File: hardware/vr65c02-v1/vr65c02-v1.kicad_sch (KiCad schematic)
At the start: 7 parts, among them J1 Conn_01x06, J2 Conn_01x06, U1 ATMEGA4809, U2 W65C02

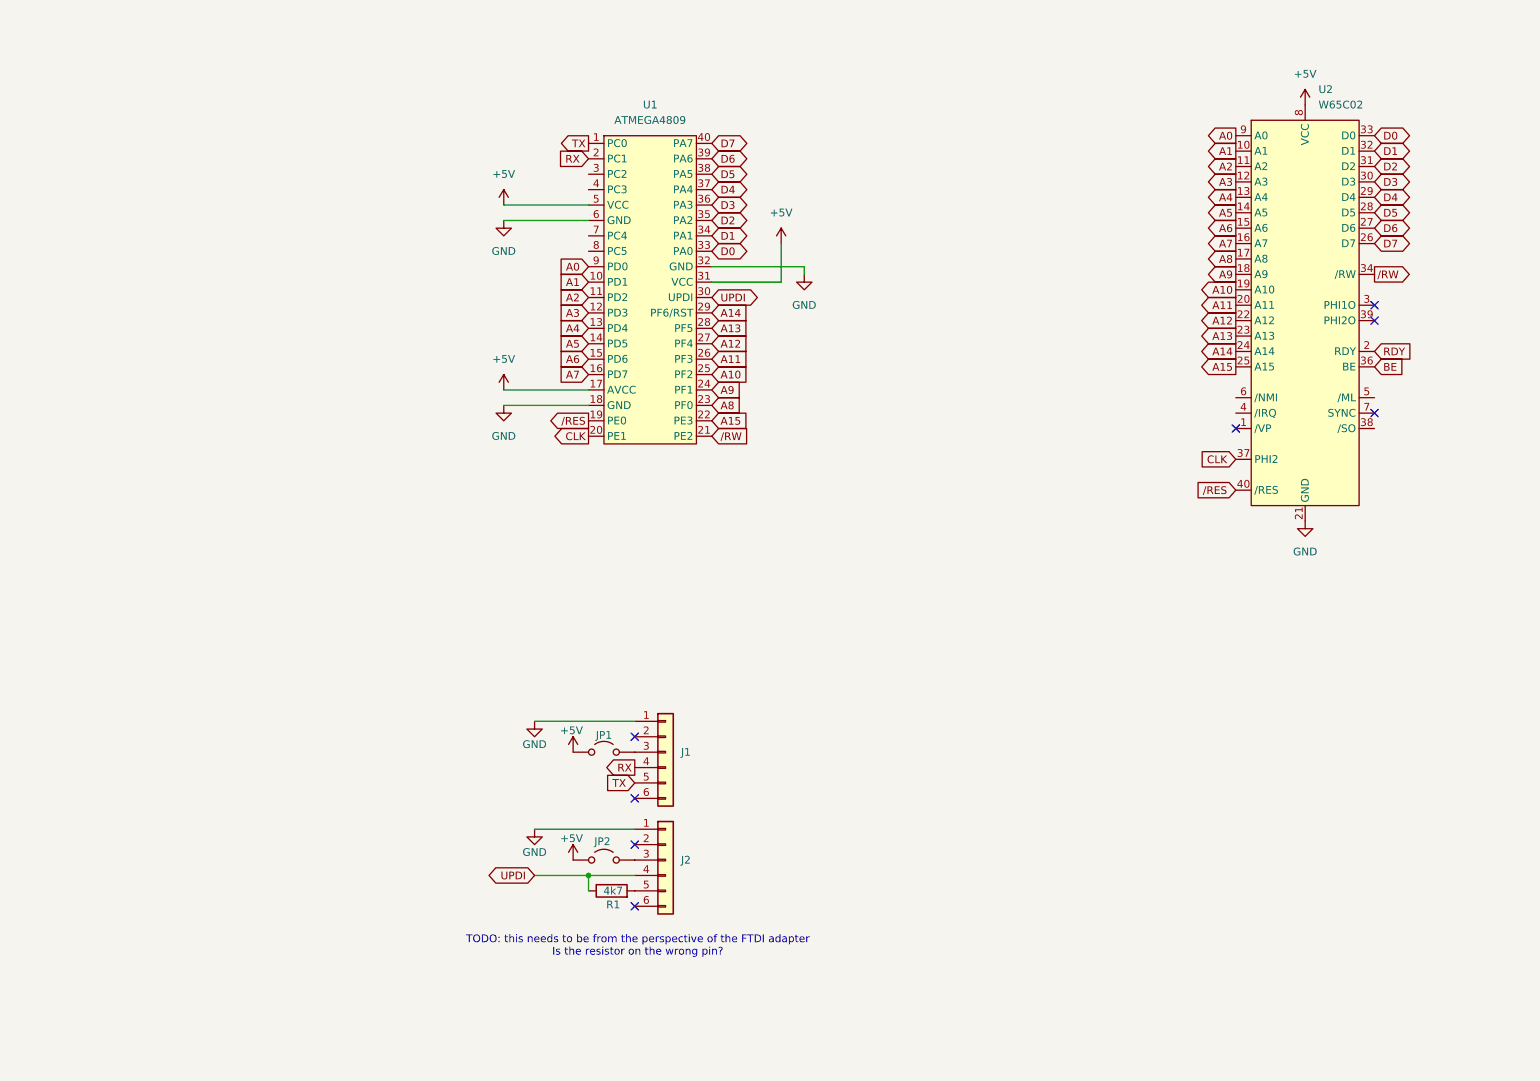
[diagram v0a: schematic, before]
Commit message: PCB v1 routed
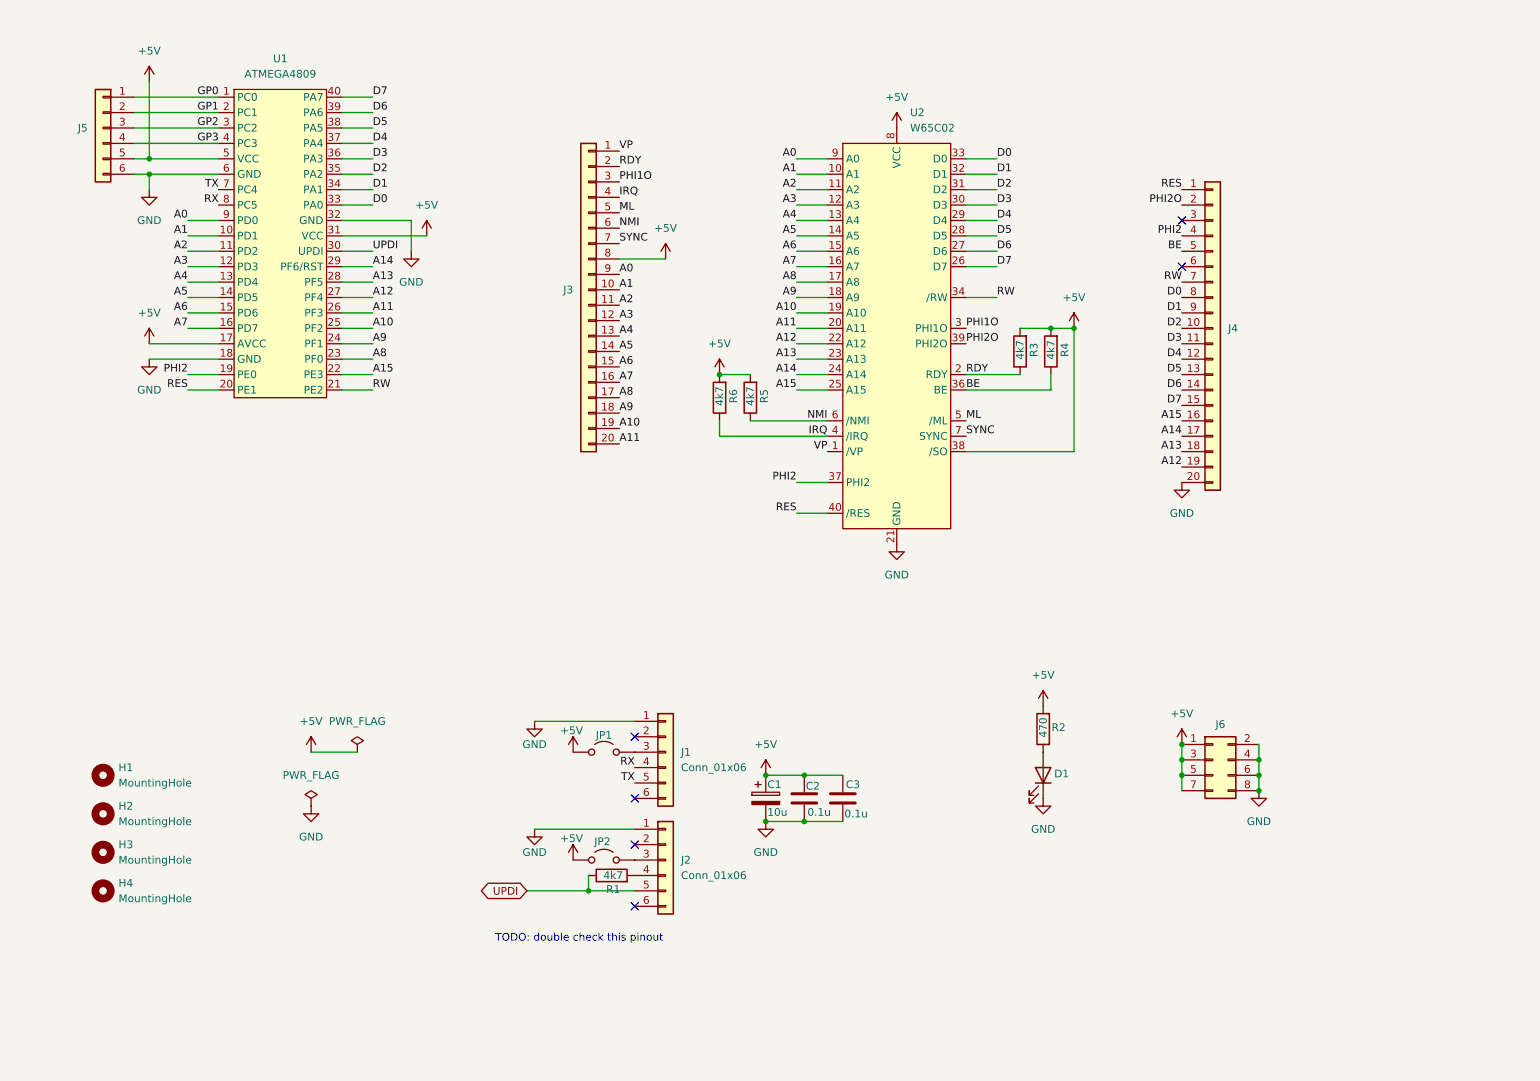
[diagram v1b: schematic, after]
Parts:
- added C1: 10u, Capacitor_THT:CP_Radial_D5.0mm_P2.50mm, symbol Device:C_Polarized
- added C2, C3: 0.1u, Capacitor_THT:C_Disc_D4.7mm_W2.5mm_P5.00mm, symbol Device:C
- added D1: LED, LED_THT:LED_D5.0mm, symbol Device:LED
- added H1, H2, H3, H4: MountingHole, MountingHole:MountingHole_3.2mm_M3, symbol Mechanical:MountingHole
- added J3, J4: Conn_01x20, Connector_PinHeader_2.54mm:PinHeader_1x20_P2.54mm_Vertical, symbol Connector_Generic:Conn_01x20
- added J5: Conn_01x06, Connector_PinHeader_2.54mm:PinHeader_1x06_P2.54mm_Vertical, symbol Connector_Generic:Conn_01x06
- added J6: Conn_02x04_Odd_Even, Connector_PinHeader_2.54mm:PinHeader_2x04_P2.54mm_Vertical, symbol Connector_Generic:Conn_02x04_Odd_Even
- added R2: 470, Resistor_THT:R_Axial_DIN0207_L6.3mm_D2.5mm_P7.62mm_Horizontal, symbol Device:R
- added R3, R4, R5, R6: 4k7, Resistor_THT:R_Axial_DIN0207_L6.3mm_D2.5mm_P7.62mm_Horizontal, symbol Device:R
- J1: footprint Connector_PinHeader_2.54mm:PinHeader_1x06_P2.54mm_Vertical -> Connector_PinSocket_2.54mm:PinSocket_1x06_P2.54mm_Vertical
- J2: footprint Connector_PinSocket_2.54mm:PinSocket_1x05_P2.54mm_Vertical -> Connector_PinSocket_2.54mm:PinSocket_1x06_P2.54mm_Vertical
- JP1, JP2: footprint TestPoint:TestPoint_2Pads_Pitch2.54mm_Drill0.8mm -> Connector_PinHeader_2.54mm:PinHeader_1x02_P2.54mm_Vertical
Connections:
- net +5V: now also U2.38 (/SO), C1.1, C2.1, C3.1, J3.8 (Pin_8), J5.5 (Pin_5), J6.1 (Pin_1), J6.3 (Pin_3), J6.5 (Pin_5), J6.7 (Pin_7), R2.2, R3.2, R4.2, R5.2, R6.2
- net A0: now also J3.9 (Pin_9)
- net A1: now also J3.10 (Pin_10)
- net A10: now also J3.19 (Pin_19)
- net A11: now also J3.20 (Pin_20)
- net A12: now also J4.19 (Pin_19)
- net A13: now also J4.18 (Pin_18)
- net A14: now also J4.17 (Pin_17)
- net A15: now also J4.16 (Pin_16)
- net A2: now also J3.11 (Pin_11)
- net A3: now also J3.12 (Pin_12)
- net A4: now also J3.13 (Pin_13)
- net A5: now also J3.14 (Pin_14)
- net A6: now also J3.15 (Pin_15)
- net A7: now also J3.16 (Pin_16)
- net A8: now also J3.17 (Pin_17)
- net A9: now also J3.18 (Pin_18)
- net BE: now also J4.5 (Pin_5), R4.1
- net D0: now also J4.8 (Pin_8)
- net D1: now also J4.9 (Pin_9)
- net D2: now also J4.10 (Pin_10)
- net D3: now also J4.11 (Pin_11)
- net D4: now also J4.12 (Pin_12)
- net D5: now also J4.13 (Pin_13)
- net D6: now also J4.14 (Pin_14)
- net D7: now also J4.15 (Pin_15)
- net GND: now also C1.2, C2.2, C3.2, D1.1 (K), J4.20 (Pin_20), J5.6 (Pin_6), J6.2 (Pin_2), J6.4 (Pin_4), J6.6 (Pin_6), J6.8 (Pin_8)
- net RDY: now also J3.2 (Pin_2), R3.1
- net RX: now also U1.8 (PC5); no longer U1.2 (PC1)
- net TX: now also U1.7 (PC4); no longer U1.1 (PC0)
- net UPDI: now also J2.5 (Pin_5); no longer J2.4 (Pin_4)
- net GP2: now reaches U1.3 (PC2)
- net GP2: now also J5.3 (Pin_3)
- net GP3: now reaches U1.4 (PC3)
- net GP3: now also J5.4 (Pin_4)
- net VP: now reaches U2.1 (/VP)
- net VP: now also J3.1 (Pin_1)
- net PHI1O: now reaches U2.3 (PHI1O)
- net PHI1O: now also J3.3 (Pin_3)
- net PHI2O: now reaches U2.39 (PHI2O)
- net PHI2O: now also J4.2 (Pin_2)
- net IRQ: now reaches U2.4 (/IRQ)
- net IRQ: now also J3.4 (Pin_4), R6.1
- net ML: now reaches U2.5 (/ML)
- net ML: now also J3.5 (Pin_5)
- net NMI: now reaches U2.6 (/NMI)
- net NMI: now also J3.6 (Pin_6), R5.1
- net SYNC: now reaches U2.7 (SYNC)
- net SYNC: now also J3.7 (Pin_7)
- net at R1.2: now also J2.4 (Pin_4); no longer J2.5 (Pin_5)
- net CLK renamed PHI2
- net PHI2: now also U1.19 (PE0), J4.4 (Pin_4); no longer U1.20 (PE1)
- net /RES renamed RES
- net RES: now also U1.20 (PE1), J4.1 (Pin_1); no longer U1.19 (PE0)
- net /RW renamed RW
- net RW: now also J4.7 (Pin_7)
- new net: D1.2 (A), R2.1
- new net GP0: J5.1 (Pin_1), U1.1 (PC0)
- new net GP1: J5.2 (Pin_2), U1.2 (PC1)
- no-connect marks 8 -> 6
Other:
- note added: "TODO: double check this pinout"
- note removed: "TODO: this needs to be from the perspective of the FTDI adapter Is the resistor on the wrong pin?"
- moved on the sheet: R1, U2

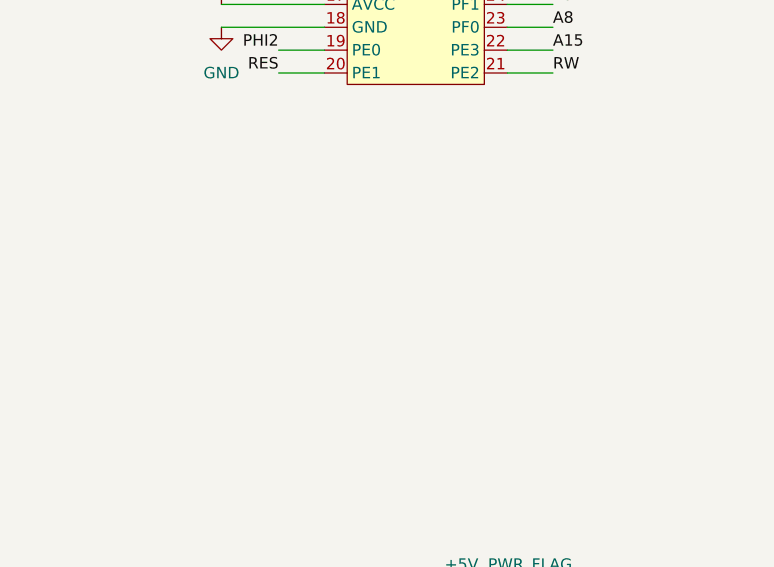
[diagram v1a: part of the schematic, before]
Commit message: Basic soft reset button option
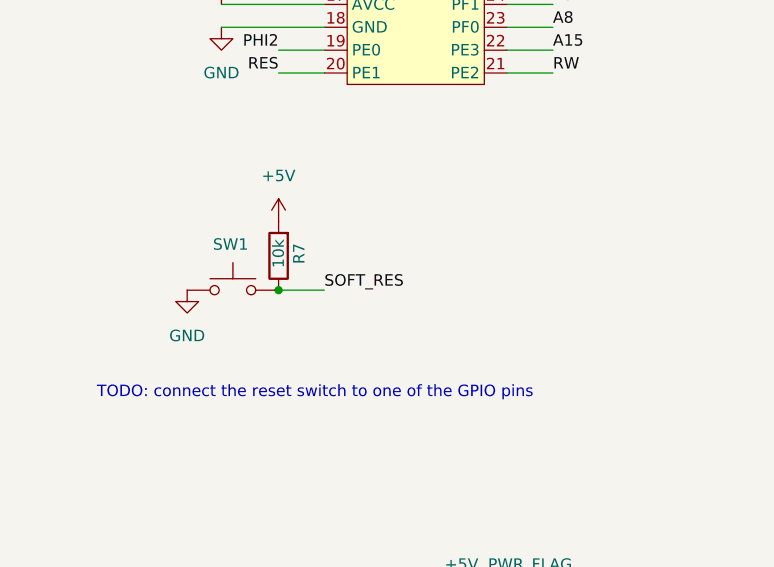
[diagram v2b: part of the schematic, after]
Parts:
- added R7: 10k, Resistor_THT:R_Axial_DIN0207_L6.3mm_D2.5mm_P7.62mm_Horizontal, symbol Device:R
- added SW1: SW_Push, Button_Switch_THT:SW_PUSH_6mm_H5mm, symbol Switch:SW_Push
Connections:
- net +5V: now also R7.2
- net GND: now also SW1.1
- new net SOFT_RES: R7.1, SW1.2
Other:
- note added: "TODO: connect the reset switch to one of the GPIO pins"

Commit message: PCB release v1.0a
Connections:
- net SOFT_RES is gone; now on net GP0: R7.1, SW1.2
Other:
- note added: "Soft Reset Switch"
- note added: "UART / Programming Headers"
- note removed: "TODO: connect the reset switch to one of the GPIO pins"
- note removed: "TODO: double check this pinout"
- company: (none) -> Colin Maykish
- title: (none) -> VR65C02
- moved on the sheet: C1, C2, C3, D1, H1, H2, H3, H4, J1, J2, J3, J4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
